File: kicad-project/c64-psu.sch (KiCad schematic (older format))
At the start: 40 parts, among them J1 Conn_01x02, J2 Conn_01x02, J3 Conn_01x02, Q1 N-MOS, U1 MAX6399, U2 LMR33630A

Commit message: replace " with ' in BOM
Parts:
- D2: MfrCode Aliexpress: \"1206 white led\" -> Aliexpress: '1206 white led'
- J1, J2, J3: MfrCode Aliexpress: \"KF301-5.0-2P\" -> Aliexpress: 'KF301-5.0-2P'
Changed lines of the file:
@@
 F 3 "" H 10200 3100 50  0001 C CNN
 F 4 "Any" H 0   0   50  0001 C CNN "Mfr"
-F 5 "Aliexpress: \"KF301-5.0-2P\"" H 0   0   50  0001 C CNN "MfrCode"
+F 5 "Aliexpress: 'KF301-5.0-2P'" H 0   0   50  0001 C CNN "MfrCode"
 	1    10200 3100
 	1    0    0    1
@@
 F 3 "" H 10100 1100 50  0001 C CNN
 F 4 "Any" H 7250 -3800 50  0001 C CNN "Mfr"
-F 5 "Aliexpress: \"KF301-5.0-2P\"" H 7250 -3800 50  0001 C CNN "MfrCode"
+F 5 "Aliexpress: 'KF301-5.0-2P'" H 7250 -3800 50  0001 C CNN "MfrCode"
 	1    10100 1100
 	1    0    0    -1
@@
 F 3 "" H 1450 1500 50  0001 C CNN
 F 4 "Any" H 0   0   50  0001 C CNN "Mfr"
-F 5 "Aliexpress: \"KF301-5.0-2P\"" H 0   0   50  0001 C CNN "MfrCode"
+F 5 "Aliexpress: 'KF301-5.0-2P'" H 0   0   50  0001 C CNN "MfrCode"
 	1    1450 1500
 	-1   0    0    1
@@
 F 3 "" H 3300 3800 50  0001 C CNN
 F 4 "Any" H 0   0   50  0001 C CNN "Mfr"
-F 5 "Aliexpress: \"1206 white led\"" H 0   0   50  0001 C CNN "MfrCode"
+F 5 "Aliexpress: '1206 white led'" H 0   0   50  0001 C CNN "MfrCode"
 	1    3300 3800
 	0    -1   -1   0

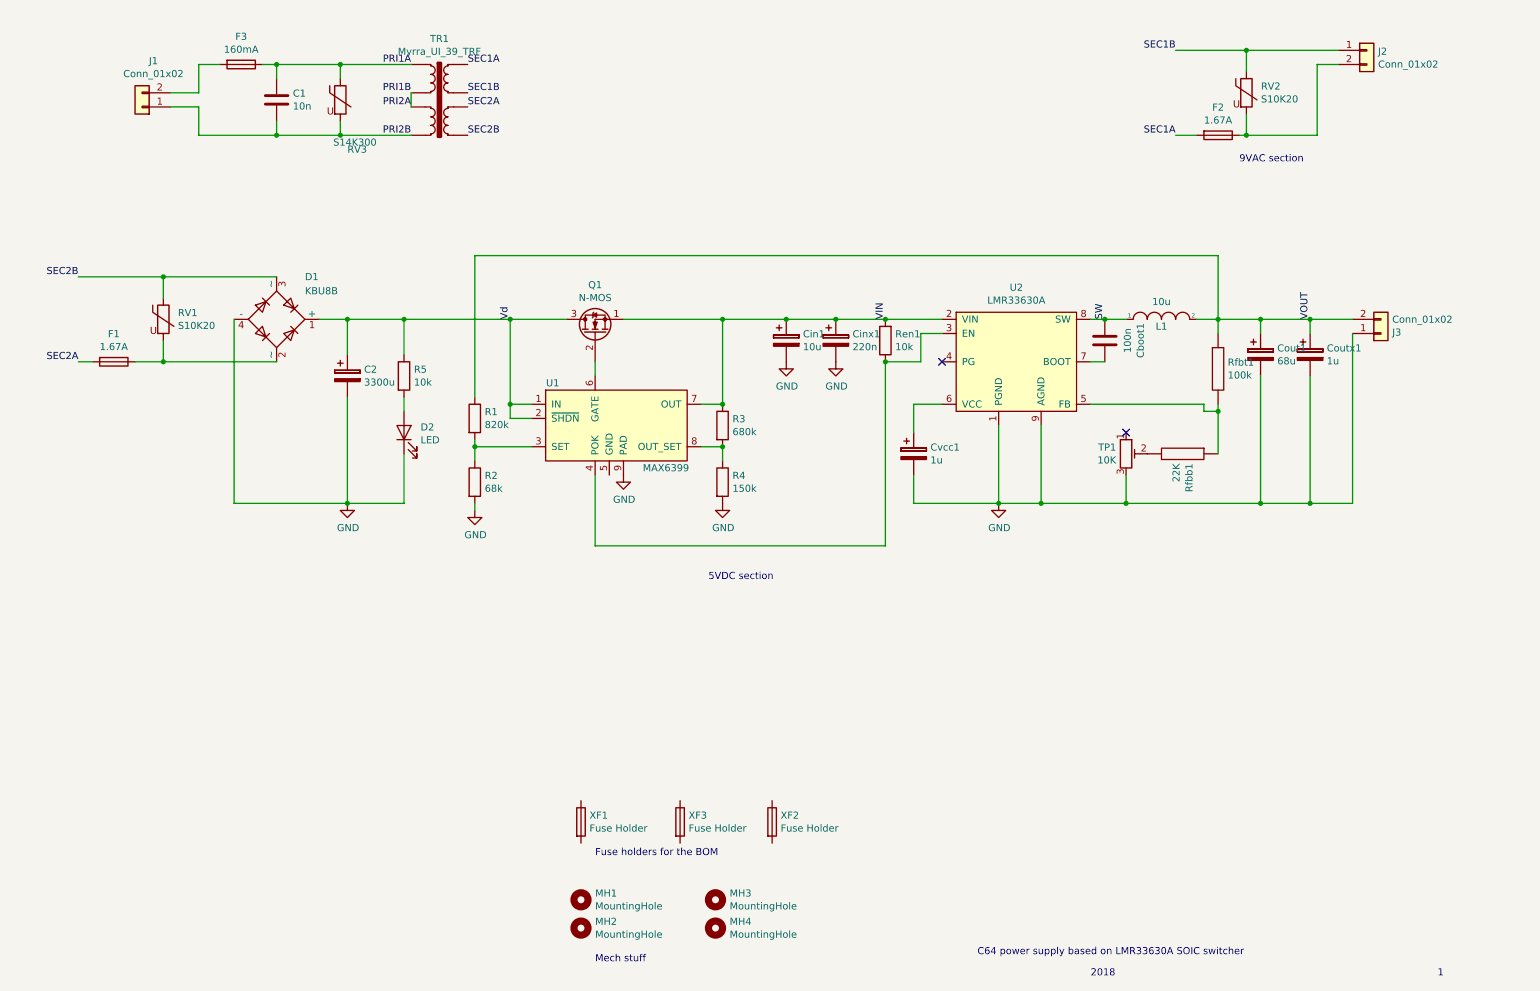
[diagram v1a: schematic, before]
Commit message: fix TR1 primary series connection (!!!), added voltage threshold comments on schematic, reversed J3 (when did that break?), added test captures,
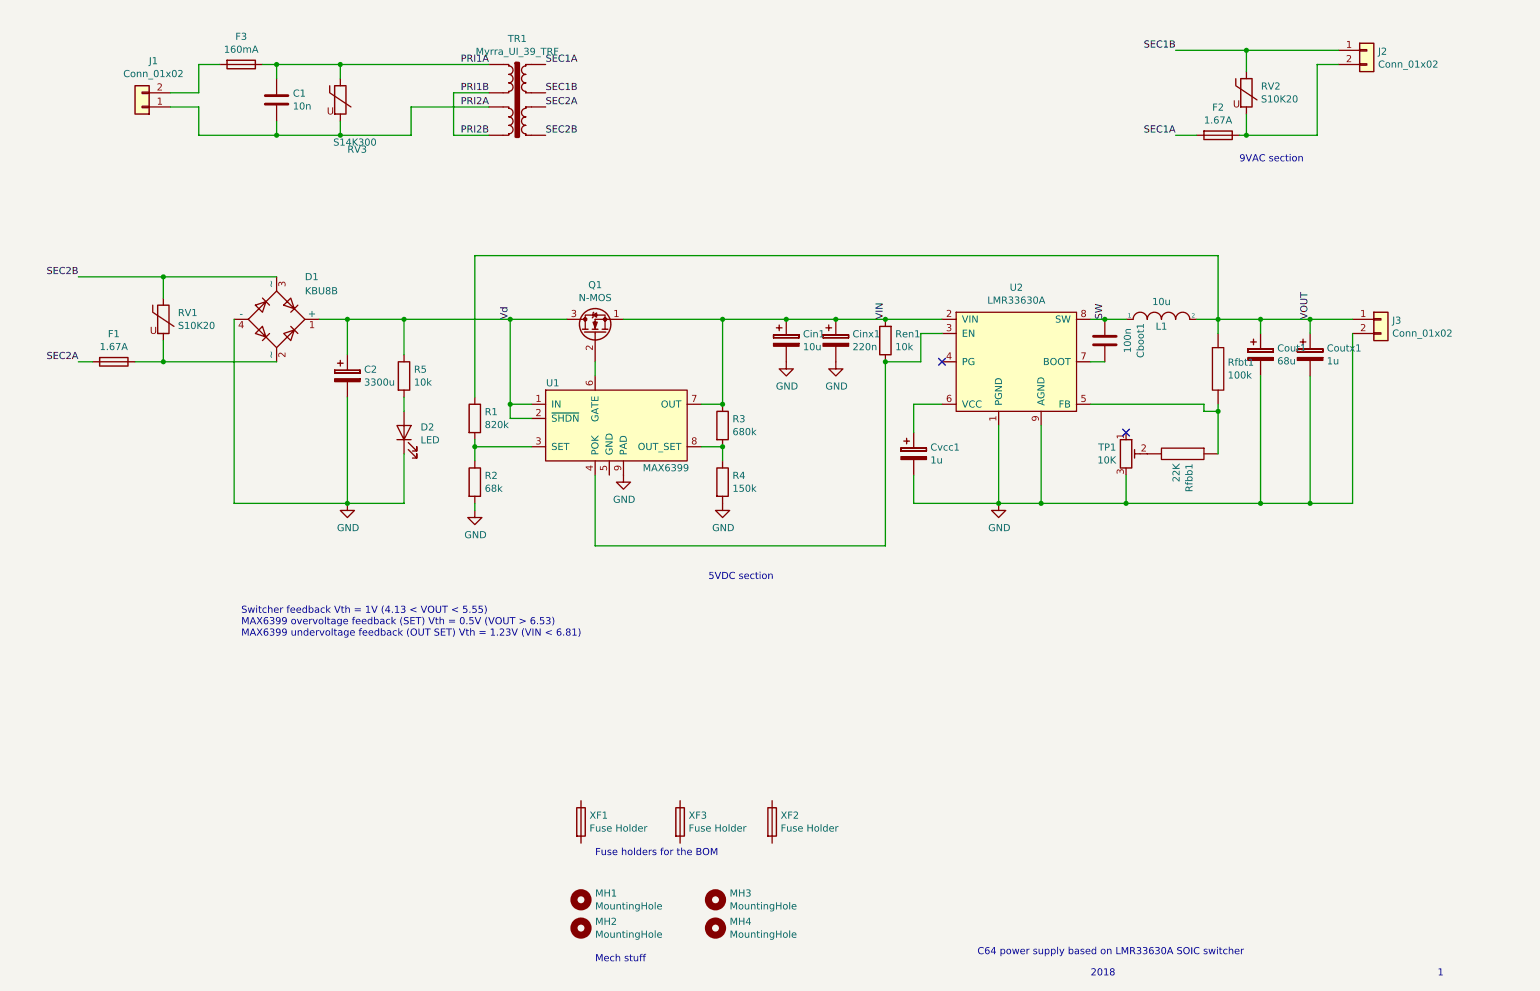
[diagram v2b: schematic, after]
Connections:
- net GND: now also J3.2 (Pin_2); no longer J3.1 (Pin_1)
- net PRI1B: now also TR1.9; no longer TR1.6
- net VOUT: now also J3.1 (Pin_1); no longer J3.2 (Pin_2)
- net PRI2B renamed PRI2A
- net PRI2A: now also TR1.6; no longer TR1.9
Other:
- note added: "Switcher feedback Vth = 1V (4.13 < VOUT < 5.55)\nMAX6399 overvoltage feedback (SET) Vth = 0.5V (VOUT > 6.53)\nMAX6399 undervoltage feedback (OUT SET) Vth = 1.23V (VIN < 6.81)"
- moved on the sheet: TR1
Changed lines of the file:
@@
 L Connector_Generic:Conn_01x02 J3
 U 1 1 5BB1E923
-P 10200 3100
-F 0 "J3" H 10280 3092 50  0000 L CNN
-F 1 "Conn_01x02" H 10280 3001 50  0000 L CNN
-F 2 "TerminalBlock_Phoenix:TerminalBlock_Phoenix_MKDS-1,5-2_1x02_P5.00mm_Horizontal" H 10200 3100 50  0001 C CNN
-F 3 "" H 10200 3100 50  0001 C CNN
-F 4 "Any" H 0   0   50  0001 C CNN "Mfr"
-F 5 "Aliexpress: 'KF301-5.0-2P'" H 0   0   50  0001 C CNN "MfrCode"
-	1    10200 3100
-	1    0    0    1
-$EndComp
-Wire Wire Line
-	10000 3100 10000 4300
+P 10200 3000
+F 0 "J3" H 10280 2992 50  0000 L CNN
+F 1 "Conn_01x02" H 10280 2901 50  0000 L CNN
+F 2 "TerminalBlock_Phoenix:TerminalBlock_Phoenix_MKDS-1,5-2_1x02_P5.00mm_Horizontal" H 10200 3000 50  0001 C CNN
+F 3 "" H 10200 3000 50  0001 C CNN
+F 4 "Any" H 0   -100 50  0001 C CNN "Mfr"
+F 5 "Aliexpress: 'KF301-5.0-2P'" H 0   -100 50  0001 C CNN "MfrCode"
+	1    10200 3000
+	1    0    0    -1
+$EndComp
 $Comp
 L Connector_Generic:Conn_01x02 J2
@@
 Connection ~ 2850 1200
 Wire Wire Line
-	2850 1200 3350 1200
+	2850 1200 3900 1200
 Wire Wire Line
 	2850 1600 2850 1700
-Connection ~ 2850 1700
-Wire Wire Line
-	2850 1700 3350 1700
 NoConn ~ 7100 3300
 Wire Wire Line
@@
 L c64-psu:Myrra_UI_39_TRF TR1
 U 1 1 5BB94271
-P 3550 1500
-F 0 "TR1" H 3550 1982 50  0000 C CNN
-F 1 "Myrra_UI_39_TRF" H 3550 1891 50  0000 C CNN
-F 2 "c64-psu:Myrra UI 39 trf" H 3550 1500 50  0001 C CNN
-F 3 "" H 3550 1500 50  0001 C CNN
-F 4 "UI 39" H 250 0   50  0001 C CNN "MfrCode"
-F 5 "Myrra" H 3550 1500 50  0001 C CNN "Mfr"
-F 6 "" H 3550 1500 50  0001 C CNN "MouserCode"
-F 7 "1777965" H 3550 1500 50  0001 C CNN "FarnellCode"
-	1    3550 1500
-	1    0    0    -1
-$EndComp
-Text Label 3350 1200 2    50   ~ 0
+P 4100 1500
+F 0 "TR1" H 4100 1982 50  0000 C CNN
+F 1 "Myrra_UI_39_TRF" H 4100 1891 50  0000 C CNN
+F 2 "c64-psu:Myrra UI 39 trf" H 4100 1500 50  0001 C CNN
+F 3 "" H 4100 1500 50  0001 C CNN
+F 4 "UI 39" H 800 0   50  0001 C CNN "MfrCode"
+F 5 "Myrra" H 4100 1500 50  0001 C CNN "Mfr"
+F 6 "" H 4100 1500 50  0001 C CNN "MouserCode"
+F 7 "1777965" H 4100 1500 50  0001 C CNN "FarnellCode"
+	1    4100 1500
+	1    0    0    -1
+$EndComp
+Text Label 3900 1200 2    50   ~ 0
 PRI1A
-Text Label 3350 1400 2    50   ~ 0
+Text Label 3900 1400 2    50   ~ 0
 PRI1B
-Text Label 3350 1500 2    50   ~ 0
+Text Label 3900 1500 2    50   ~ 0
 PRI2A
-Text Label 3350 1700 2    50   ~ 0
+Text Label 3900 1700 2    50   ~ 0
 PRI2B
 Text Label 8750 1700 2    50   ~ 0
@@
 	3300 3950 3300 4300
 Wire Wire Line
-	3350 1400 3350 1500
-Wire Wire Line
 	2100 4300 2900 4300
 Connection ~ 2900 3000
@@
 	1    0    0    -1
 $EndComp
-Text Label 3750 1200 0    50   ~ 0
+Text Label 4300 1200 0    50   ~ 0
 SEC1A
-Text Label 3750 1400 0    50   ~ 0
+Text Label 4300 1400 0    50   ~ 0
 SEC1B
-Text Label 3750 1500 0    50   ~ 0
+Text Label 4300 1500 0    50   ~ 0
 SEC2A
-Text Label 3750 1700 0    50   ~ 0
+Text Label 4300 1700 0    50   ~ 0
 SEC2B
 Text Notes 4650 7550 0    50   ~ 0
@@
 Text Notes 5450 4850 0    50   ~ 0
 5VDC section
+Wire Wire Line
+	2850 1700 3350 1700
+Wire Wire Line
+	3350 1700 3350 1500
+Wire Wire Line
+	3350 1500 3900 1500
+Connection ~ 2850 1700
+Wire Wire Line
+	3900 1400 3650 1400
+Wire Wire Line
+	3650 1400 3650 1700
+Wire Wire Line
+	3650 1700 3900 1700
+Wire Wire Line
+	10000 3100 10000 4300
+Text Notes 2150 5250 0    50   ~ 0
+Switcher feedback Vth = 1V (4.13 < VOUT < 5.55)\nMAX6399 overvoltage feedback (SET) Vth = 0.5V (VOUT > 6.53)\nMAX6399 undervoltage feedback (OUT SET) Vth = 1.23V (VIN < 6.81)
 $EndSCHEMATC

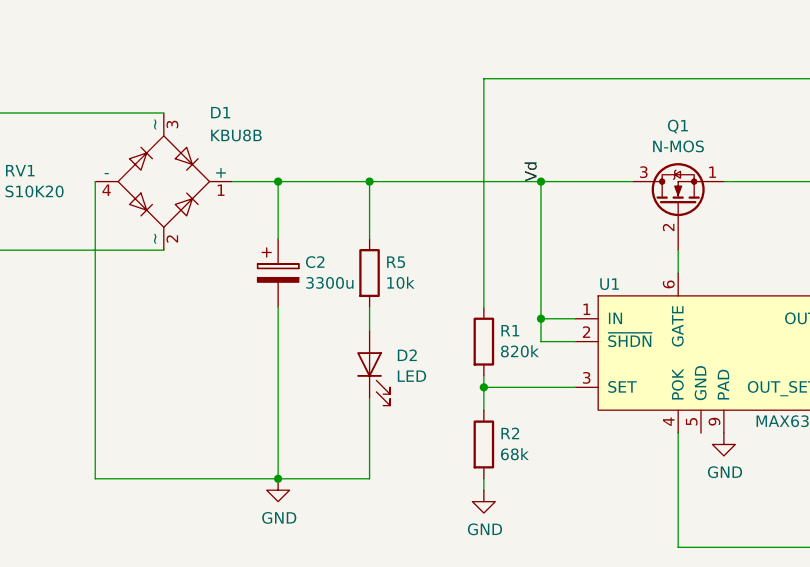
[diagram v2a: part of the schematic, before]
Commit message: fix R5 value and MfrCode
(was a 1206 10K but MfrCode was of a 0805 470 resistor). Also lowered original value of 10K to 4K7 to balance LED power waste vs overvoltage latch reset time
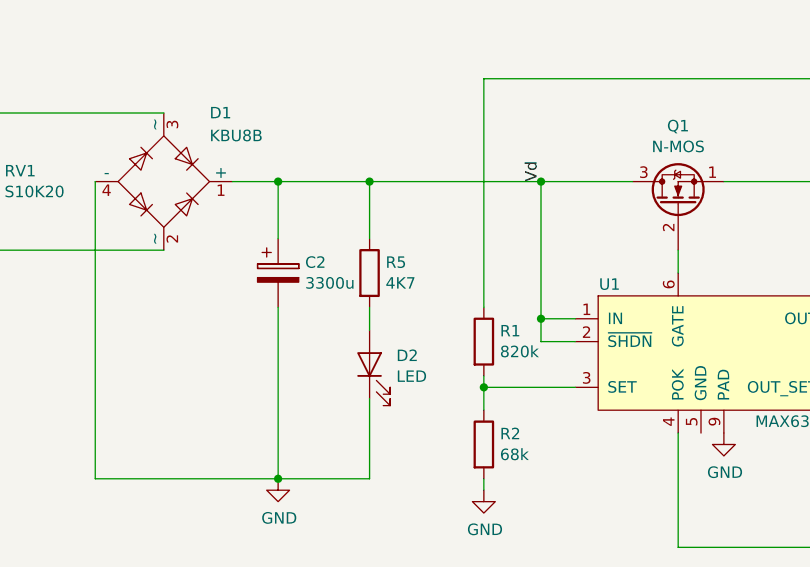
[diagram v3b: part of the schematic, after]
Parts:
- R5: value 10k -> 4K7; MfrCode CR0805-FX-4700ELF -> CR1206-FX-4701ELF; MouserCode 652-CR0805FX-4700ELF -> 652-CR1206FX-4701ELF
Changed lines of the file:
@@
 P 3300 3400
 F 0 "R5" H 3370 3446 50  0000 L CNN
-F 1 "10k" H 3370 3355 50  0000 L CNN
+F 1 "4K7" H 3370 3355 50  0000 L CNN
 F 2 "Resistor_SMD:R_1206_3216Metric_Pad1.42x1.75mm_HandSolder" V 3230 3400 50  0001 C CNN
 F 3 "" H 3300 3400 50  0001 C CNN
-F 4 "CR0805-FX-4700ELF" H 0   0   50  0001 C CNN "MfrCode"
+F 4 "CR1206-FX-4701ELF" H 0   0   50  0001 C CNN "MfrCode"
 F 5 "Bourns" H 0   0   50  0001 C CNN "Mfr"
-F 6 "652-CR0805FX-4700ELF" H 0   0   50  0001 C CNN "MouserCode"
+F 6 "652-CR1206FX-4701ELF" H 0   0   50  0001 C CNN "MouserCode"
 	1    3300 3400
 	1    0    0    -1
